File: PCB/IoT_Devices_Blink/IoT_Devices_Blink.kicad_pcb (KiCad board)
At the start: 2 copper layers, 34.5 x 26.5 mm, 6 parts, among them J1 Conn_01x07_Socket, J2 Conn_01x07_Socket, SW1 SW_Push

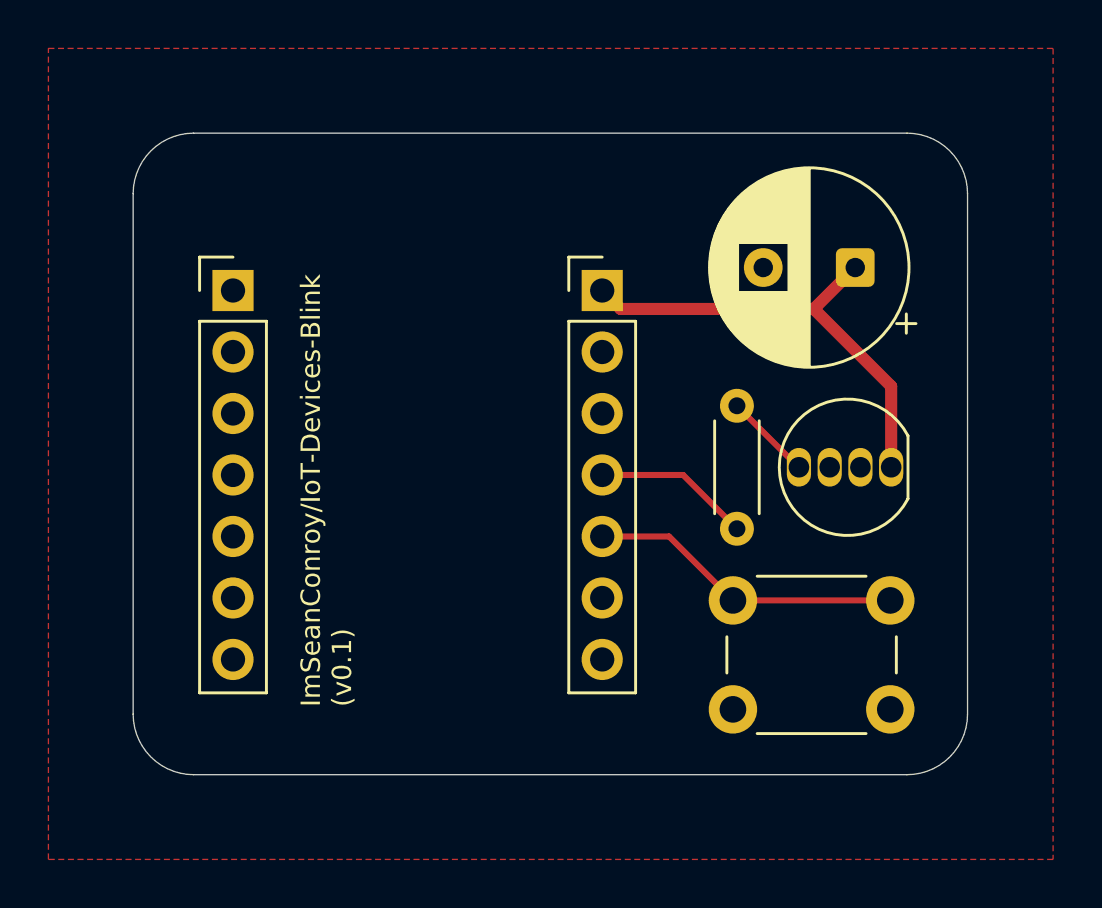
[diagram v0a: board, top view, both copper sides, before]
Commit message: Create basic blink iot dashboard
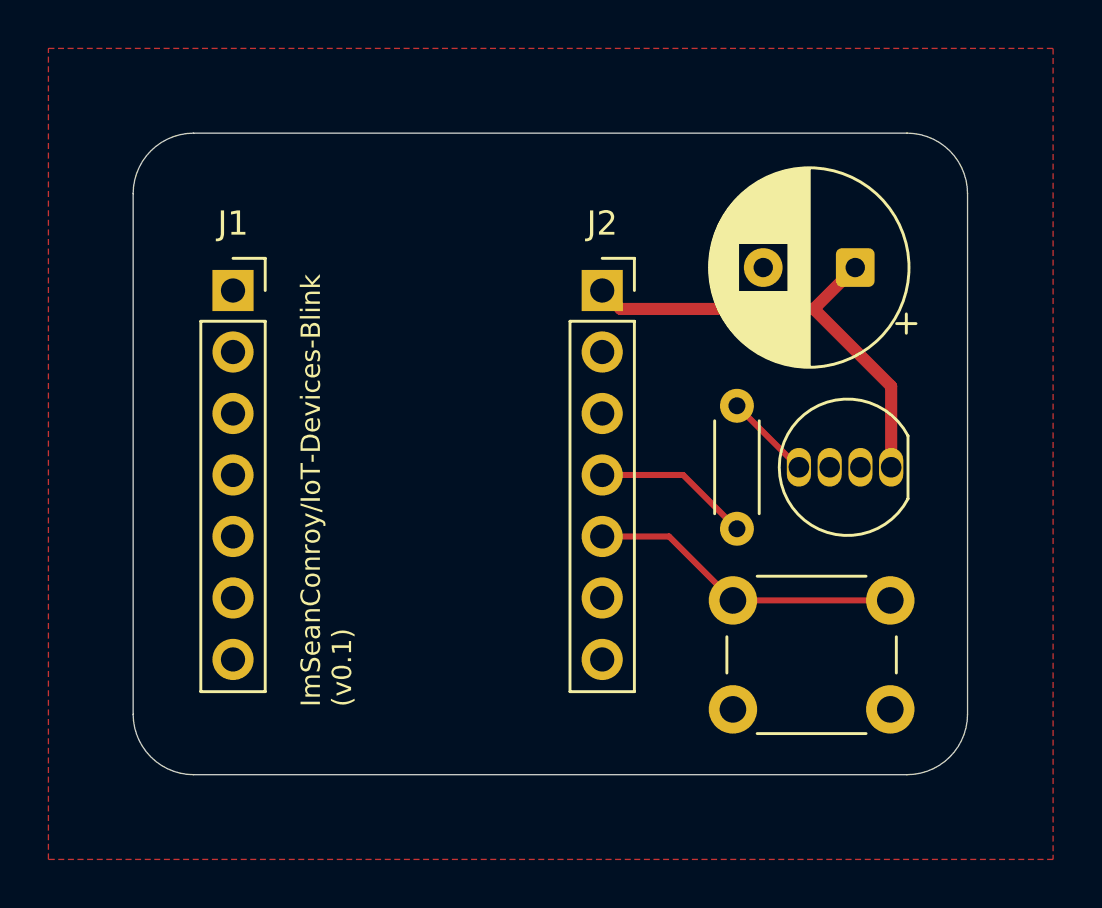
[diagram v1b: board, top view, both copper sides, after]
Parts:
- J1, J2: footprint Connector_PinHeader_2.54mm:PinHeader_1x07_P2.54mm_Vertical -> Connector_PinSocket_2.54mm:PinSocket_1x07_P2.54mm_Vertical
